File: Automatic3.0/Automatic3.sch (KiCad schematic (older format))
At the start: 64 parts, among them J10 Encoder, J11 UART0, J12 Bluetooth, J13 Compass, J14 CONN_01X06, J15 I/O PINS, J16 CONN_01X01, J17 CONN_01X01, J18 CONN_01X01, J19 CONN_01X01, J2 CONN_02X04, J3 Motor, J4 Jumper, J5 USB_B, J6 Jumper, J7 Bluetooth, J8 Line Tracker and Proximity, J9 Reset_jumper, SW1 SW_Push, SW2 SW_Push, U3 Arduino_Mega2560_Shield, U4 ATMEGA88A-PU, Y1 Crystal

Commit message: Created new schemetic for automatic
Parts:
- removed C13, C7: 22, modFiles:Capacitor_Disc_Small, symbol C
- removed D7: LED, modFiles:LED_D3.0mm, symbol LED
- removed J11: UART0, Pin_Headers:Pin_Header_Straight_1x02_Pitch2.54mm, symbol CONN_01X02
- removed J12, J7: Bluetooth, Pin_Headers:Pin_Header_Straight_1x04_Pitch2.54mm, symbol CONN_01X04
- removed J13: Compass, Pin_Headers:Pin_Header_Straight_1x04_Pitch2.54mm, symbol CONN_01X04
- removed J4, J6: Jumper, Pin_Headers:Pin_Header_Straight_1x02_Pitch2.54mm, symbol CONN_01X02
- removed J9: Reset_jumper, Pin_Headers:Pin_Header_Straight_1x03_Pitch2.54mm, symbol CONN_01X03
- removed R15, R7: 10K, modFiles:Resistor_small, symbol R
- removed R22: 150, modFiles:Resistor_small, symbol R
- removed R23, R26, R27, R28, R29, R30, R31, R32, R33, R34, R35, R8: 10k, modFiles:Resistor_small, symbol R
- removed SW1, SW2: SW_Push, modFiles:Push_Button, symbol SW_Push
- removed U4: ATMEGA88A-PU, modFiles:DIP-28, symbol ATMEGA88A-PU
- removed Y1: Crystal, modFiles:Crystal, symbol Crystal
- added D4: D_Zener, Diodes_THT:D_DO-35_SOD27_P7.62mm_Horizontal, symbol D_Zener
- added J11: Compass, Pin_Headers:Pin_Header_Straight_1x04_Pitch2.54mm, symbol CONN_01X04
- added J12: Bluetooth, Pin_Headers:Pin_Header_Straight_1x06_Pitch2.54mm, symbol CONN_01X06
- added J6, J9: I/O Pins, Pin_Headers:Pin_Header_Straight_1x08_Pitch2.54mm, symbol CONN_01X08
- added U2: Arduino_Mega2560_Shield, modFiles:Arduino_Mega2560_Shield, symbol Arduino_Mega2560_Shield
- J14: value CONN_01X06 -> Bluetooth
- renumbered C6 to C1, C14 to C2, C8 to C3, C9 to C4, C10 to C5, C11 to C6, C12 to C7, D9 to D1, D8 to D2, D11 to D3, J15 to J1, J8 to J10, J10 to J13, J3 to J15, J16 to J2, J2 to J3, J17 to J4, J18 to J5, J5 to J7, J19 to J8, R5 to R1, R18 to R10, R19 to R11, R20 to R12, R21 to R13, R9 to R2, R10 to R3, R11 to R4, R12 to R5, R13 to R6, R14 to R7, R16 to R8, R17 to R9, U3 to U1
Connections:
- net labels added: INT, PC0, PC1, PC5, PC7, PK0, RESET1, SCL, SDA
- net labels removed: 3V3, OC3A, PA6, PA7, PB0, PD7, PF0, PF1, PF2, PF3, PF4, PF5, PF6, PF7, PG1, PL6, PL7
- wire segments 108 -> 67
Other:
- moved on the sheet: C1, C2, C3, C4, C5, C6, C7, D1, D2, D3, J1, J10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

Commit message: Modified the automatic circuit
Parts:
- removed C4: 0.1uF, modFiles:Capacitor_Disc_Medium, symbol C
- removed J1: I/O PINS, Pin_Headers:Pin_Header_Straight_1x03_Pitch2.54mm, symbol CONN_01X03
- added C12, C15, C16, C17: 104, modFiles:Capacitor_Disc_Medium, symbol C
- added R23, R24: 10k, modFiles:Resistor_small, symbol R
- C1, C3, C5, C6: value 0.1uF -> 104
- C2, C7: value C -> 104
- J3: value CONN_02X04 -> GND VCC
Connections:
- net labels added: RX1, SINT2, SINT3, SINT4, SINT5, TX1
- net labels removed: INT0, INT1, INT3, INT4, PB5, PB6, PB7, RESET
- wire segments 67 -> 78
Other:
- moved on the sheet: C2, J10, J13, J15

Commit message: modified the automatic circuit
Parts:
- removed J3: GND VCC, Pin_Headers:Pin_Header_Straight_2x04_Pitch2.54mm, symbol CONN_02X04
- added D14, D16, D17: LED, modFiles:LED_D3.0mm, symbol LED
- added D15: D_Zener, Diodes_THT:D_DO-35_SOD27_P7.62mm_Horizontal, symbol D_Zener
- added J1: CONN_02X05, Pin_Headers:Pin_Header_Straight_2x05_Pitch2.54mm, symbol CONN_02X05
- added J19: Bluetooth, Pin_Headers:Pin_Header_Straight_1x06_Pitch2.54mm, symbol CONN_01X06
- added R25, R26, R27: 1, modFiles:Resistor_small, symbol R
- added R28, R29, R30: R, modFiles:Resistor_small, symbol R
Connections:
- net labels added: SRX3, STX3
- net labels removed: RX1, TX1
- wire segments 78 -> 89
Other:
- moved on the sheet: R1

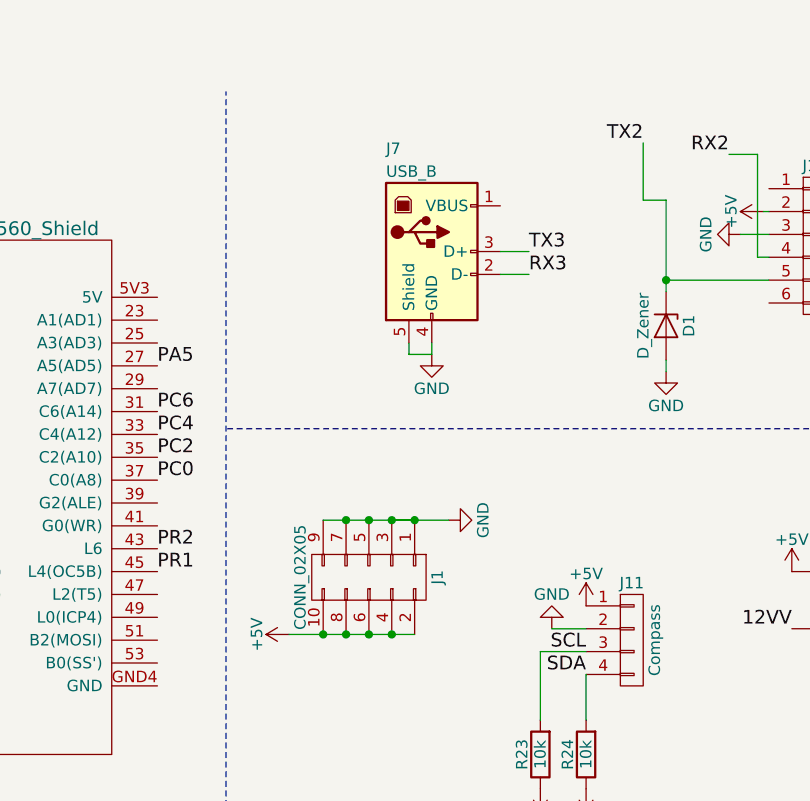
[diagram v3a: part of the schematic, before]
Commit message: added the jst connector
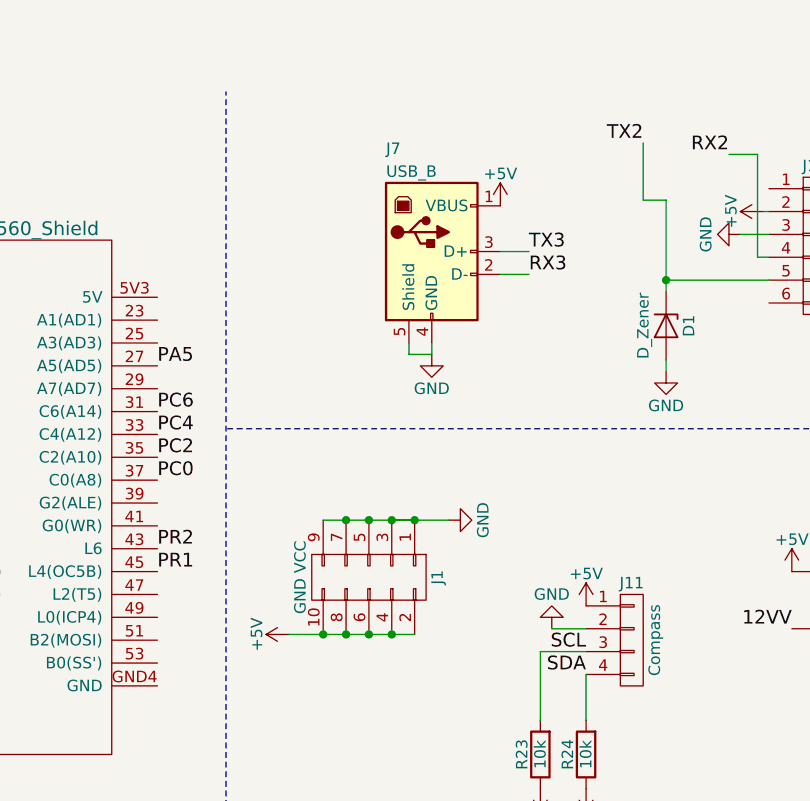
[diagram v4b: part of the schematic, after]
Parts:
- J1: value CONN_02X05 -> GND VCC
- J11: footprint Pin_Headers:Pin_Header_Straight_1x04_Pitch2.54mm -> Connectors_JST:JST_PH_B4B-PH-K_04x2.00mm_Straight
- J7: footprint modFiles:Connector_USB -> Connectors_JST:JST_PH_B4B-PH-K_04x2.00mm_Straight
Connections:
- net +5V: now also J7.1 (VBUS)
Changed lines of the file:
@@
 LIBS:contrib
 LIBS:valves
-LIBS:Prashant_library
 LIBS:74xgxx
 LIBS:ac-dc
@@
 LIBS:ftdi
 LIBS:gennum
-LIBS:graphic
 LIBS:hc11
 LIBS:ir
 LIBS:Lattice
 LIBS:leds
-LIBS:logo
 LIBS:maxim
 LIBS:mechanical
@@
 LIBS:zetex
 LIBS:Zilog
+LIBS:Prashant_library
 LIBS:Automatic3-cache
 EELAYER 25 0
@@
 F 0 "J7" H 6225 1625 50  0000 L CNN
 F 1 "USB_B" H 6225 1525 50  0000 L CNN
-F 2 "modFiles:Connector_USB" H 6575 1125 50  0001 C CNN
+F 2 "Connectors_JST:JST_PH_B4B-PH-K_04x2.00mm_Straight" H 6575 1125 50  0001 C CNN
 F 3 "" H 6575 1125 50  0001 C CNN
 	1    6425 1175
@@
 F 0 "J11" H 7300 3125 50  0000 C CNN
 F 1 "Compass" V 7400 2875 50  0000 C CNN
-F 2 "Pin_Headers:Pin_Header_Straight_1x04_Pitch2.54mm" H 7300 2875 50  0001 C CNN
+F 2 "Connectors_JST:JST_PH_B4B-PH-K_04x2.00mm_Straight" H 7300 2875 50  0001 C CNN
 F 3 "" H 7300 2875 50  0001 C CNN
 	1    7300 2875
@@
 P 6150 2600
 F 0 "J1" H 6150 2900 50  0000 C CNN
-F 1 "CONN_02X05" H 6150 2300 50  0000 C CNN
+F 1 "GND VCC" H 6150 2300 50  0000 C CNN
 F 2 "Pin_Headers:Pin_Header_Straight_2x05_Pitch2.54mm" H 6150 1400 50  0001 C CNN
 F 3 "" H 6150 1400 50  0001 C CNN
@@
 Wire Wire Line
 	1325 325  1525 325
+$Comp
+L +5V #PWR043
+U 1 1 5B273E9C
+P 6725 975
+F 0 "#PWR043" H 6725 825 50  0001 C CNN
+F 1 "+5V" H 6725 1115 50  0000 C CNN
+F 2 "" H 6725 975 50  0001 C CNN
+F 3 "" H 6725 975 50  0001 C CNN
+	1    6725 975
+	1    0    0    -1
+$EndComp
 $EndSCHEMATC

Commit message: modified the automatic circuit
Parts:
- removed C12: 104, modFiles:Capacitor_Disc_Medium, symbol C
- removed D15, D4: D_Zener, Diodes_THT:D_DO-35_SOD27_P7.62mm_Horizontal, symbol D_Zener
- removed D16, D17: LED, modFiles:LED_D3.0mm, symbol LED
- removed J19: Bluetooth, Pin_Headers:Pin_Header_Straight_1x06_Pitch2.54mm, symbol CONN_01X06
- removed J6: I/O Pins, Pin_Headers:Pin_Header_Straight_1x08_Pitch2.54mm, symbol CONN_01X08
- removed R29, R30: R, modFiles:Resistor_small, symbol R
- added D18: D_Zener, Diodes_THT:D_DO-35_SOD27_P7.62mm_Horizontal, symbol D_Zener
- added D4: LED, modFiles:LED_D3.0mm, symbol LED
- added J19, J21: CONN_01X02, modFiles:Connector_Bornier_2, symbol CONN_01X02
- added J20: Bluetooth, Pin_Headers:Pin_Header_Straight_1x06_Pitch2.54mm, symbol CONN_01X06
- added J6: Zone_Switches, modFiles:Connector_DB_9, symbol DB9_Female_MountingHoles
- added Q2, Q3: IRF540N, modFiles:Voltage_Regulators, symbol IRF540N
- added R31, R32, R33, R34: R, modFiles:Resistor_small, symbol R
- added R36, R37: 560, modFiles:Resistor_small, symbol R
- added R38, R39: 10k, modFiles:Resistor_small, symbol R
- D2, D3: footprint modFiles:Diode_Small -> modFiles:Diode_small
- J11: footprint Connectors_JST:JST_PH_B4B-PH-K_04x2.00mm_Straight -> Connectors_JST:JST_XH_B04B-XH-A_04x2.50mm_Straight
- J2, J4, J5, J8: footprint Connectors:1pin -> modFiles:1_Pin
- J7: value USB_B -> Throwing; footprint Connectors_JST:JST_PH_B4B-PH-K_04x2.00mm_Straight -> Connectors_JST:JST_XH_B04B-XH-A_04x2.50mm_Straight
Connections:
- net +5V: now also J20.2 (P2), R32.1, R33.1, R34.1; no longer C6.1, J11.1 (P1), R23.1, R24.1
- net 5VV: no longer U1.5V1 (5V)
- net GND: now also D18.2 (A), D4.1 (K), J20.3 (P3), J6.0 (PAD), J6.6, Q2.3 (S), Q3.3 (S), R38.2, R39.2
- net PR1: now also R34.2
- net PR2: now also R33.2
- net RX2: no longer J12.4 (P4)
- net RX3: now also J12.4 (P4)
- net SCL: no longer U2.SCL (DO(INT0))
- net SDA: no longer U2.SDA (D1(INT1))
- net SRX3: now also J20.4 (P4)
- net STX3: now also D18.1 (K), J20.5 (P5)
- net TX2: no longer D1.1 (K), J12.5 (P5)
- net TX3: now also D1.1 (K), J12.5 (P5)
- net 3V3: now reaches U1.3V3
- net 3V3: now also C6.1, J11.1 (P1), R23.1, R24.1
- net PF0: now reaches U1.A0 (F0)
- net PF0: now also J6.8
- net PF1: now reaches U1.A1 (F1)
- net PF1: now also J6.9
- net PF2: now reaches U1.A2 (F2)
- net PF2: now also J6.5
- net PF3: now reaches U1.A3 (F3)
- net PF3: now also J6.4
- net PF4: now reaches U1.A4 (F4)
- net PF4: now also J6.3
- net PF5: now reaches U1.A5 (F5)
- net PF5: now also J6.2
- net PF6: now reaches U1.A6 (F6)
- net PF6: now also J6.1, R32.2
- net PF7: now reaches U1.A7 (F7)
- net at U2.13 (B7(OC0A-0C1C)): now also R31.2
- new net: D4.2 (A), R31.1
- new net: Q2.1 (G), R36.1, R38.1
- new net: J19.2 (P2), Q2.2 (D)
- new net: Q3.1 (G), R37.1, R39.1
- new net: J21.2 (P2), Q3.2 (D)
- new net 12Vin: J19.1 (P1), J21.1 (P1)
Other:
- moved on the sheet: C1, C15, C16, C17, C2, C3, C5, C6, C7, D1, D2, D3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

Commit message: Almost final automatic base mega + bridge
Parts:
- removed D1, D18: D_Zener, Diodes_THT:D_DO-35_SOD27_P7.62mm_Horizontal, symbol D_Zener
- removed J1: GND VCC, Pin_Headers:Pin_Header_Straight_2x05_Pitch2.54mm, symbol CONN_02X05
- removed J11: Compass, Connectors_JST:JST_XH_B04B-XH-A_04x2.50mm_Straight, symbol CONN_01X04
- removed J14: Bluetooth, Pin_Headers:Pin_Header_Straight_1x06_Pitch2.54mm, symbol CONN_01X06
- removed J19, J21: CONN_01X02, modFiles:Connector_Bornier_2, symbol CONN_01X02
- removed J7: Throwing, Connectors_JST:JST_XH_B04B-XH-A_04x2.50mm_Straight, symbol USB_B
- removed J9: I/O Pins, Pin_Headers:Pin_Header_Straight_1x08_Pitch2.54mm, symbol CONN_01X08
- removed Q2, Q3: IRF540N, modFiles:Voltage_Regulators, symbol IRF540N
- removed R27: 1, modFiles:Resistor_small, symbol R
- removed R36, R37: 560, modFiles:Resistor_small, symbol R
- removed R38, R39: 10k, modFiles:Resistor_small, symbol R
- added C11, C8: 10uf, modFiles:Capacitor_10uF, symbol C
- added C12, C14: 104, modFiles:Capacitor_Disc_Medium, symbol C
- added J1: GND_VCC, Pin_Headers:Pin_Header_Straight_2x03_Pitch2.54mm, symbol Conn_02x03_Odd_Even
- added J11, J14, J19, J21, J22: J, modFiles:Jumper, symbol J
- added J23: BUCK+LLC, modFiles:BUCK+LLC, symbol Conn_01x12
- added J24: CONN_01X01, modFiles:1_Pin, symbol CONN_01X01
- added J25: JST, Connectors_JST:JST_XH_B04B-XH-A_04x2.50mm_Straight, symbol Conn_01x04
- added J3: Compass & throwing, modFiles:Connector_DB_9, symbol DB9_Female_MountingHoles
- added J7: Conn_01x04, Pin_Headers:Pin_Header_Straight_1x04_Pitch2.54mm, symbol Conn_01x04
- added J9: I/O_PINS, Pin_Headers:Pin_Header_Straight_1x05_Pitch2.54mm, symbol Conn_01x05
- R1: value 1 -> 15K
- R25, R26: value 1 -> 10K
- R32, R33, R34: value R -> 10K
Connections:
- net +5V: now also R25.1, J1.2 (Pin_2), J1.4 (Pin_4), J1.6 (Pin_6), J21.1 (2), J23.3 (Pin_3), J3.3; no longer R26.2, R32.1
- net 12VVD: now also J25.3 (Pin_3); no longer J10.12 (P12)
- net 3V3: now also J3.2
- net GND: now also R32.1, C11.1, C12.2, C14.1, C8.2, J1.1 (Pin_1), J1.3 (Pin_3), J1.5 (Pin_5), J11.1 (2), J14.1 (2), J19.1 (2), J22.1 (2), J23.1 (Pin_1), J25.4 (Pin_4), J3.0 (PAD), J3.7; no longer R25.1, R25.2, U1.GND5 (GND)
- net JP2: now also J10.12 (P12); no longer J10.13 (P13)
- net PF6: no longer J6.1, R32.2
- net PR1: now also J23.4 (Pin_4); no longer R34.2, U1.45 (L4(OC5B))
- net PR2: now also J23.5 (Pin_5); no longer R33.2, U1.43 (L6)
- net RX0: now also J25.1 (Pin_1)
- net RX2: now also J25.2 (Pin_2); no longer U2.16 (H1(TX2))
- net RX3: now also J3.8
- net SCL: now also J3.6
- net SDA: now also J3.1
- net TX3: now also J3.9
- net PR3o: now reaches U1.47 (L2(T5))
- net PR3o: now also R32.2, J23.9 (Pin_9)
- net L2: now reaches U1.5 (E3(AIN1-OC3A))
- net L2: now also R26.2, C11.2, C14.2, J3.5
- net L1: now reaches U1.6 (H3(OC4A))
- net L1: now also R25.2, C12.1, C8.1, J3.4
- net LED2: now reaches U1.A10 (K2)
- net LED2: now also J23.11 (Pin_11)
- net at U1.A11 (K3): now also J7.4 (Pin_4)
- net at U1.A12 (K4): now also J7.3 (Pin_3)
- net at U1.A13 (K5): now also J7.2 (Pin_2)
- net at U1.A14 (K6): now also J7.1 (Pin_1)
- net LED1: now reaches U1.A9 (K1)
- net LED1: now also J23.10 (Pin_10)
- net at U2.A0 (F0): now also J9.5 (Pin_5)
- net at U2.A1 (F1): now also J9.4 (Pin_4)
- net at U2.A2 (F2): now also J9.3 (Pin_3)
- net at U2.A3 (F3): now also J9.2 (Pin_2)
- net at U2.A4 (F4): now also J9.1 (Pin_1)
- new net +12V: J23.2 (Pin_2)
- new net PR1o: J23.7 (Pin_7), R34.2, U1.45 (L4(OC5B))
- new net PR2o: J23.8 (Pin_8), R33.2, U1.43 (L6)
- new net PR3: J10.13 (P13), J23.6 (Pin_6)
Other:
- moved on the sheet: C1, C15, C16, C17, C2, C3, C5, C6, C7, D2, D3, J12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
